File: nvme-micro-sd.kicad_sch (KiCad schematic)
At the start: 32 parts, among them J501 Bus_M.2_1-2199230-6, J502 MicroSD_1140084168, M501 Mech_M2_2280_H2.5mm

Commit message: [#53901] Update symbols & footprints from lib
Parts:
- D503: value LED_R_0603_598-8D80-107F -> LED_G; footprint antmicro-footprints:LED_0603_1608Metric_R -> antmicro-footprints:LED_0603_1608Metric_G; symbol antmicroLEDIndicationDiscrete:LED_R_0603_598-8D80-107F -> antmicroLEDIndicationDiscrete:LED_G_0603_598-8D80-107F
- M501, TP501, TP502, TP503, TP504: now left out of the parts list
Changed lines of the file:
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@@
   (title_block
     (title "CM4 Baseboard")
-    (date "2024-03-14")
+    (date "2024-03-22")
     (rev "1.0.0")
     (company "Antmicro")
@@
   )
   (symbol (lib_id "antmicroModules:Mech_M2_2280_H2.5mm") (at 234.95 121.92 180) (unit 1)
-    (in_bom yes) (on_board yes) (dnp no) (fields_autoplaced)
+    (in_bom no) (on_board yes) (dnp no) (fields_autoplaced)
     (property "Reference" "M501" (at 229.87 107.95 0)
       (effects (font (size 1.27 1.27)))
@@
   )
   (symbol (lib_id "antmicroTestPoints:TP_0.75mm_SMD") (at 204.47 76.2 0) (mirror x) (unit 1)
-    (in_bom yes) (on_board yes) (dnp no)
+    (in_bom no) (on_board yes) (dnp no)
     (property "Reference" "TP503" (at 212.09 76.2 0)
       (effects (font (size 1.27 1.27)))
@@
   )
   (symbol (lib_id "antmicroTestPoints:TP_0.75mm_SMD") (at 204.47 73.66 0) (mirror x) (unit 1)
-    (in_bom yes) (on_board yes) (dnp no)
+    (in_bom no) (on_board yes) (dnp no)
     (property "Reference" "TP502" (at 212.09 73.66 0)
       (effects (font (size 1.27 1.27)))
@@
   )
   (symbol (lib_id "antmicroTestPoints:TP_0.75mm_SMD") (at 204.47 78.74 0) (mirror x) (unit 1)
-    (in_bom yes) (on_board yes) (dnp no)
+    (in_bom no) (on_board yes) (dnp no)
     (property "Reference" "TP504" (at 212.09 78.74 0)
       (effects (font (size 1.27 1.27)))
@@
   )
   (symbol (lib_id "antmicroTestPoints:TP_0.75mm_SMD") (at 204.47 59.69 0) (mirror x) (unit 1)
-    (in_bom yes) (on_board yes) (dnp no)
+    (in_bom no) (on_board yes) (dnp no)
     (property "Reference" "TP501" (at 207.01 57.15 0)
       (effects (font (size 1.27 1.27)))
@@
   )
   (symbol (lib_id "antmicroTVSDiodes:TPD1E0B04_XDFN-2") (at 285.75 198.12 270) (mirror x) (unit 1)
-    (in_bom yes) (on_board yes) (dnp no)
-    (property "Reference" "D504" (at 288.29 194.3099 90)
+    (in_bom yes) (on_board yes) (dnp no) (fields_autoplaced)
+    (property "Reference" "D504" (at 288.29 194.31 90)
       (effects (font (size 1.27 1.27)) (justify left))
     )
     (property "Value" "TPD1E0B04_XDFN-2" (at 288.29 196.8499 90)
-      (effects (font (size 1.27 1.27)) (justify left))
+      (effects (font (size 1.27 1.27)) (justify left) hide)
     )
     (property "Footprint" "antmicro-footprints:XDFN-2_1x0.60mm" (at 290.83 193.04 0)
@@
       (effects (font (size 1.524 1.524)) (justify left bottom) hide)
     )
-    (property "MPN" "TPD1E0B04DPYR" (at 298.45 193.04 0)
-      (effects (font (size 1.524 1.524)) (justify left bottom) hide)
+    (property "MPN" "TPD1E0B04DPYR" (at 288.29 196.85 90)
+      (effects (font (size 1.524 1.524)) (justify left))
     )
     (property "Author" "Antmicro" (at 270.51 182.88 0)
@@
     )
     (property "Value" "MicroSD_1140084168" (at 257.175 194.31 0)
-      (effects (font (size 1.27 1.27) (thickness 0.15)))
+      (effects (font (size 1.27 1.27) (thickness 0.15)) hide)
     )
     (property "Footprint" "antmicro-footprints:MicroSD_Amphenol_1140084168" (at 281.94 208.28 0)
@@
       (effects (font (size 1.27 1.27) (thickness 0.15)) (justify left bottom) hide)
     )
-    (property "MPN" "1140084168" (at 281.94 213.36 0)
-      (effects (font (size 1.27 1.27) (thickness 0.15)) (justify left bottom) hide)
+    (property "MPN" "1140084168" (at 257.175 194.31 0)
+      (effects (font (size 1.27 1.27) (thickness 0.15)))
     )
     (property "Manufacturer" "Amphenol" (at 281.94 215.9 0)
@@
     )
   )
-  (symbol (lib_id "antmicroLEDIndicationDiscrete:LED_R_0603_598-8D80-107F") (at 217.17 90.17 90) (mirror x) (unit 1)
+  (symbol (lib_id "antmicroLEDIndicationDiscrete:LED_G_0603_598-8D80-107F") (at 217.17 90.17 90) (mirror x) (unit 1)
     (in_bom yes) (on_board yes) (dnp no) (fields_autoplaced)
-    (property "Reference" "D503" (at 219.71 94.2974 90)
+    (property "Reference" "D503" (at 219.71 93.0275 90)
       (effects (font (size 1.27 1.27) (thickness 0.15)) (justify right))
     )
-    (property "Value" "LED_R_0603_598-8D80-107F" (at 214.63 85.09 0)
-      (effects (font (size 1.27 1.27) (thickness 0.15)) (justify left bottom) hide)
+    (property "Value" "LED_G" (at 219.71 95.5675 90)
+      (effects (font (size 1.27 1.27) (thickness 0.15)) (justify right))
     )
-    (property "Footprint" "antmicro-footprints:LED_0603_1608Metric_R" (at 224.79 113.03 0)
+    (property "Footprint" "antmicro-footprints:LED_0603_1608Metric_G" (at 224.79 113.03 0)
       (effects (font (size 1.27 1.27) (thickness 0.15)) (justify left bottom) hide)
     )

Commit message: [#56708] Add loclib
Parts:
- C501, C503, C505: footprint antmicro-footprints:C_0402_1005Metric -> cm4-baseboard-footprints:C_0402_1005Metric; symbol antmicroCapacitors0402:C_10u_0402 -> cm4-baseboard:C_10u_0402
- C502, C504, C506, C507: footprint antmicro-footprints:C_0402_1005Metric -> cm4-baseboard-footprints:C_0402_1005Metric; symbol antmicroCapacitors0402:C_1u_0402 -> cm4-baseboard:C_1u_0402
- D501, D502: footprint antmicro-footprints:Nexperia_DFN-10_2.5x1mm_P0.5mm -> cm4-baseboard-footprints:Nexperia_DFN-10_2.5x1mm_P0.5mm; symbol antmicroTVSDiodes:PUSB3F96X_PASS -> cm4-baseboard:PUSB3F96X_PASS
- D503: footprint antmicro-footprints:LED_0603_1608Metric_G -> cm4-baseboard-footprints:LED_0603_1608Metric_G; symbol antmicroLEDIndicationDiscrete:LED_G_0603_598-8D80-107F -> cm4-baseboard:LED_G_0603_598-8D80-107F
- D504: footprint antmicro-footprints:XDFN-2_1x0.60mm -> cm4-baseboard-footprints:XDFN-2_1x0.60mm; symbol antmicroTVSDiodes:TPD1E0B04_XDFN-2 -> cm4-baseboard:TPD1E0B04_XDFN-2
- H501: footprint antmicro-footprints:Spacer_Drill3.7mm_H2.5mm_9774025151R -> cm4-baseboard-footprints:Spacer_Drill3.7mm_H2.5mm_9774025151R; symbol antmicroMechanicalParts:Spacer_Drill3.7mm_H2.5mm_9774025151R -> cm4-baseboard:Spacer_Drill3.7mm_H2.5mm_9774025151R
- J501: footprint antmicro-footprints:Bus_M.2_Socket_Key_M_TE_1-2199230-6 -> cm4-baseboard-footprints:Bus_M.2_Socket_Key_M_TE_1-2199230-6; symbol antmicroPciConnectors:Bus_M.2_1-2199230-6 -> cm4-baseboard:Bus_M.2_1-2199230-6
- J502: footprint antmicro-footprints:MicroSD_Amphenol_1140084168 -> cm4-baseboard-footprints:MicroSD_Amphenol_1140084168; symbol antmicroMemoryConnectorsPCCardSockets:MicroSD_1140084168 -> cm4-baseboard:MicroSD_1140084168
- M501: footprint antmicro-footprints:Mech_M2_2280_H2.5mm -> cm4-baseboard-footprints:Mech_M2_2280_H2.5mm; symbol antmicroModules:Mech_M2_2280_H2.5mm -> cm4-baseboard:Mech_M2_2280_H2.5mm
- R501, R502, R503, R504, R506, R507, R508, R509, R511, R513: footprint antmicro-footprints:R_0402_1005Metric -> cm4-baseboard-footprints:R_0402_1005Metric; symbol antmicroResistors0402:R_10k_0402 -> cm4-baseboard:R_10k_0402
- R505, R512: footprint antmicro-footprints:R_0402_1005Metric -> cm4-baseboard-footprints:R_0402_1005Metric; symbol antmicroResistors0402:R_470R_0402 -> cm4-baseboard:R_470R_0402
- R510: footprint antmicro-footprints:R_0402_1005Metric -> cm4-baseboard-footprints:R_0402_1005Metric; symbol antmicroResistors0402:R_200R_0402 -> cm4-baseboard:R_200R_0402
- TP501, TP502, TP503, TP504: footprint antmicro-footprints:TP_SMD_0.75mm -> cm4-baseboard-footprints:TP_SMD_0.75mm; symbol antmicroTestPoints:TP_0.75mm_SMD -> cm4-baseboard:TP_0.75mm_SMD

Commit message: [#56708] Update symbol/footprint props; Update modules visibilty
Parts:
- D503: value LED_G -> LED_G_0603_598-8D80-107F; Color (none) -> Green
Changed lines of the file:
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@@
       (effects (font (size 1.27 1.27) (thickness 0.15)) (justify right))
     )
-    (property "Value" "LED_G" (at 219.71 95.5675 90)
-      (effects (font (size 1.27 1.27) (thickness 0.15)) (justify right))
-    )
-    (property "Footprint" "cm4-baseboard-footprints:LED_0603_1608Metric_G" (at 224.79 113.03 0)
+    (property "Value" "LED_G_0603_598-8D80-107F" (at 224.79 113.03 0)
       (effects (font (size 1.27 1.27) (thickness 0.15)) (justify left bottom) hide)
     )
-    (property "Datasheet" "https://www.farnell.com/datasheets/3093797.pdf" (at 227.33 113.03 0)
+    (property "Footprint" "cm4-baseboard-footprints:LED_0603_1608Metric_G" (at 227.33 113.03 0)
       (effects (font (size 1.27 1.27) (thickness 0.15)) (justify left bottom) hide)
     )
-    (property "MPN" "598-8D80-107F" (at 229.87 113.03 0)
+    (property "Datasheet" "https://www.farnell.com/datasheets/3093797.pdf" (at 229.87 113.03 0)
       (effects (font (size 1.27 1.27) (thickness 0.15)) (justify left bottom) hide)
     )
-    (property "Manufacturer" "Dialight" (at 232.41 113.03 0)
+    (property "MPN" "598-8D80-107F" (at 232.41 113.03 0)
       (effects (font (size 1.27 1.27) (thickness 0.15)) (justify left bottom) hide)
     )
-    (property "Author" "Antmicro" (at 234.95 113.03 0)
+    (property "Manufacturer" "Dialight" (at 234.95 113.03 0)
       (effects (font (size 1.27 1.27) (thickness 0.15)) (justify left bottom) hide)
     )
-    (property "License" "Apache-2.0" (at 237.49 113.03 0)
+    (property "Author" "Antmicro" (at 237.49 113.03 0)
       (effects (font (size 1.27 1.27) (thickness 0.15)) (justify left bottom) hide)
     )
+    (property "License" "Apache-2.0" (at 240.03 113.03 0)
+      (effects (font (size 1.27 1.27) (thickness 0.15)) (justify left bottom) hide)
+    )
+    (property "Color" "Green" (at 219.71 95.5675 90)
+      (effects (font (size 1.27 1.27)) (justify right))
+    )
     (pin "1")

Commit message: [#57456] Remove loclib
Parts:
- C501, C503, C505: footprint cm4-baseboard-footprints:C_0402_1005Metric -> antmicro-footprints:C_0402_1005Metric; symbol cm4-baseboard:C_10u_0402 -> antmicroCapacitors0402:C_10u_0402
- C502, C504, C506, C507: footprint cm4-baseboard-footprints:C_0402_1005Metric -> antmicro-footprints:C_0402_1005Metric; symbol cm4-baseboard:C_1u_0402 -> antmicroCapacitors0402:C_1u_0402
- D501, D502: footprint cm4-baseboard-footprints:Nexperia_DFN-10_2.5x1mm_P0.5mm -> antmicro-footprints:Nexperia_DFN-10_2.5x1mm_P0.5mm; symbol cm4-baseboard:PUSB3F96X_PASS -> antmicroTVSDiodes:PUSB3F96X_PASS
- D503: footprint cm4-baseboard-footprints:LED_0603_1608Metric_G -> antmicro-footprints:LED_0603_1608Metric_G; symbol cm4-baseboard:LED_G_0603_598-8D80-107F -> antmicroLEDIndicationDiscrete:LED_G_0603_598-8D80-107F
- D504: footprint cm4-baseboard-footprints:XDFN-2_1x0.60mm -> antmicro-footprints:XDFN-2_1x0.60mm; symbol cm4-baseboard:TPD1E0B04_XDFN-2 -> antmicroTVSDiodes:TPD1E0B04_XDFN-2
- H501: footprint cm4-baseboard-footprints:Spacer_Drill3.7mm_H2.5mm_9774025151R -> antmicro-footprints:Spacer_Drill3.7mm_H2.5mm_9774025151R; symbol cm4-baseboard:Spacer_Drill3.7mm_H2.5mm_9774025151R -> antmicroMechanicalParts:Spacer_Drill3.7mm_H2.5mm_9774025151R
- J501: footprint cm4-baseboard-footprints:Bus_M.2_Socket_Key_M_TE_1-2199230-6 -> antmicro-footprints:Bus_M.2_Socket_Key_M_TE_1-2199230-6; symbol cm4-baseboard:Bus_M.2_1-2199230-6 -> antmicroPciConnectors:Bus_M.2_1-2199230-6
- J502: footprint cm4-baseboard-footprints:MicroSD_Amphenol_1140084168 -> antmicro-footprints:MicroSD_Amphenol_1140084168; symbol cm4-baseboard:MicroSD_1140084168 -> antmicroMemoryConnectorsPCCardSockets:MicroSD_1140084168
- M501: footprint cm4-baseboard-footprints:Mech_M2_2280_H2.5mm -> antmicro-footprints:Mech_M2_2280_H2.5mm; symbol cm4-baseboard:Mech_M2_2280_H2.5mm -> antmicroModules:Mech_M2_2280_H2.5mm
- R501, R502, R503, R504, R506, R507, R508, R509, R511, R513: footprint cm4-baseboard-footprints:R_0402_1005Metric -> antmicro-footprints:R_0402_1005Metric; symbol cm4-baseboard:R_10k_0402 -> antmicroResistors0402:R_10k_0402
- R505, R512: footprint cm4-baseboard-footprints:R_0402_1005Metric -> antmicro-footprints:R_0402_1005Metric; symbol cm4-baseboard:R_470R_0402 -> antmicroResistors0402:R_470R_0402
- R510: footprint cm4-baseboard-footprints:R_0402_1005Metric -> antmicro-footprints:R_0402_1005Metric; symbol cm4-baseboard:R_200R_0402 -> antmicroResistors0402:R_200R_0402
- TP501, TP502, TP503, TP504: footprint cm4-baseboard-footprints:TP_SMD_0.75mm -> antmicro-footprints:TP_SMD_0.75mm; symbol cm4-baseboard:TP_0.75mm_SMD -> antmicroTestPoints:TP_0.75mm_SMD

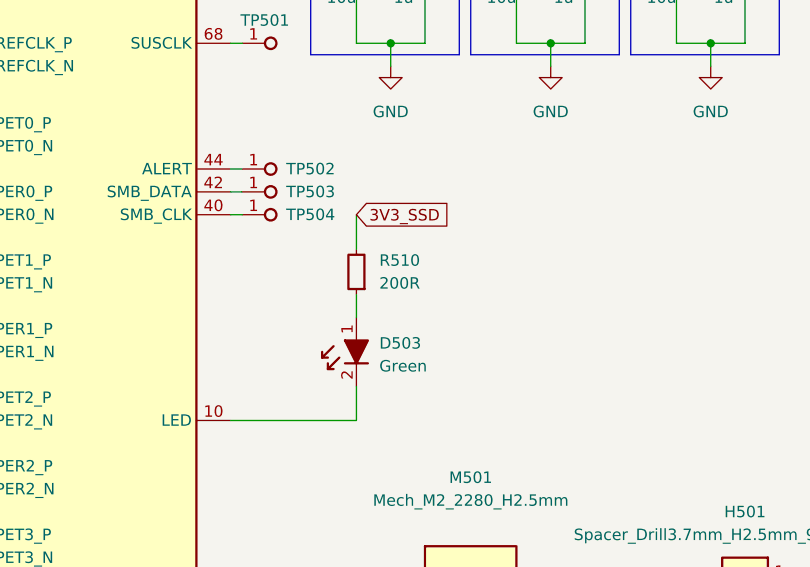
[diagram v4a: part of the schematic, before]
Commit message: [#58122] LED related fixes & improvements
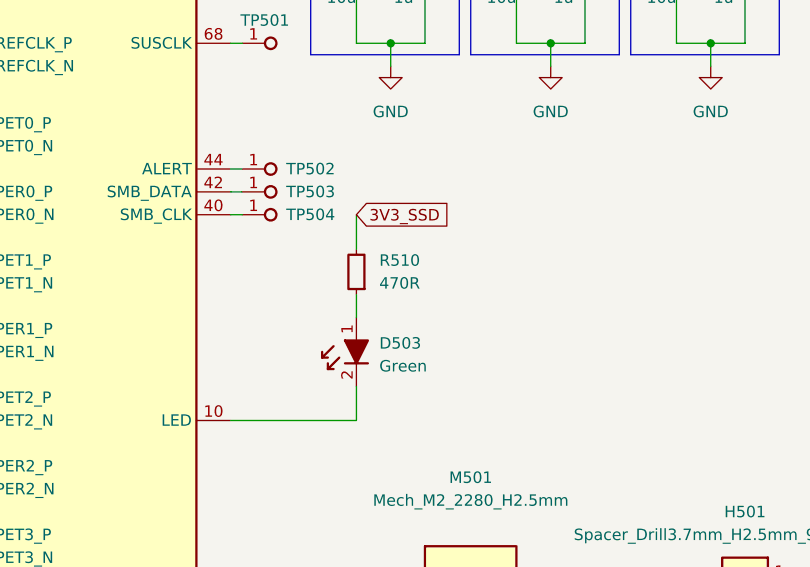
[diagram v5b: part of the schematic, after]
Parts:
- R510: value R_200R_0402 -> R_470R_0402; symbol antmicroResistors0402:R_200R_0402 -> antmicroResistors0402:R_470R_0402; MPN CR0402-FX-2000GLF -> CR0402-FX-4700GLF; Val 200R -> 470R
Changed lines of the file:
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@@
     )
   )
-  (symbol (lib_id "antmicroResistors0402:R_200R_0402") (at 217.17 87.63 270) (mirror x) (unit 1)
+  (symbol (lib_id "antmicroResistors0402:R_470R_0402") (at 217.17 87.63 270) (mirror x) (unit 1)
     (in_bom yes) (on_board yes) (dnp no) (fields_autoplaced)
     (property "Reference" "R510" (at 219.71 83.8199 90)
       (effects (font (size 1.27 1.27)) (justify left))
     )
-    (property "Value" "R_200R_0402" (at 204.47 67.31 0)
+    (property "Value" "R_470R_0402" (at 204.47 67.31 0)
       (effects (font (size 1.27 1.27) (thickness 0.15)) (justify left bottom) hide)
     )
@@
       (effects (font (size 1.27 1.27) (thickness 0.15)) (justify left bottom) hide)
     )
-    (property "MPN" "CR0402-FX-2000GLF" (at 196.85 67.31 0)
+    (property "MPN" "CR0402-FX-4700GLF" (at 196.85 67.31 0)
       (effects (font (size 1.27 1.27) (thickness 0.15)) (justify left bottom) hide)
     )
-    (property "Val" "200R" (at 219.71 86.3599 90)
+    (property "Val" "470R" (at 219.71 86.3599 90)
       (effects (font (size 1.27 1.27) (thickness 0.15)) (justify left))
     )
